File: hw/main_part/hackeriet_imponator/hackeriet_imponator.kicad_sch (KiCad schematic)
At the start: 9 parts, among them U1 ATmega328PB-A

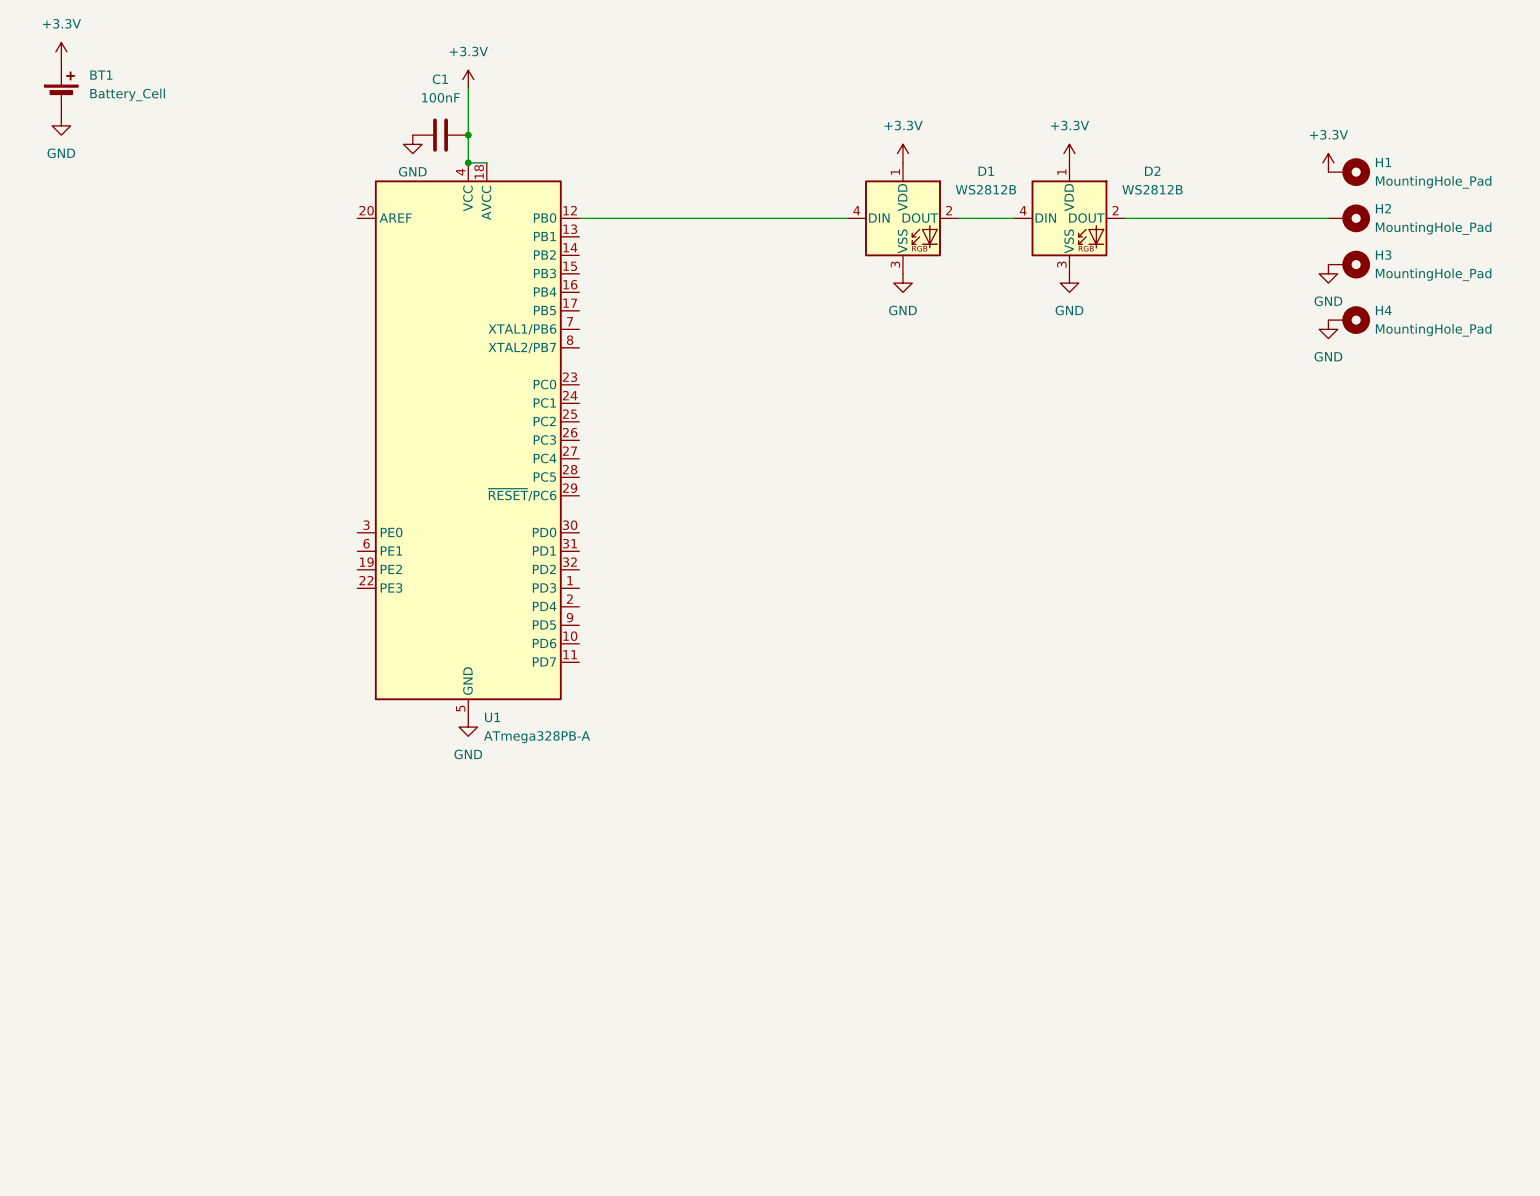
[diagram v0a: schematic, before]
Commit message: Added ring. Added programming header. Started with batt connector
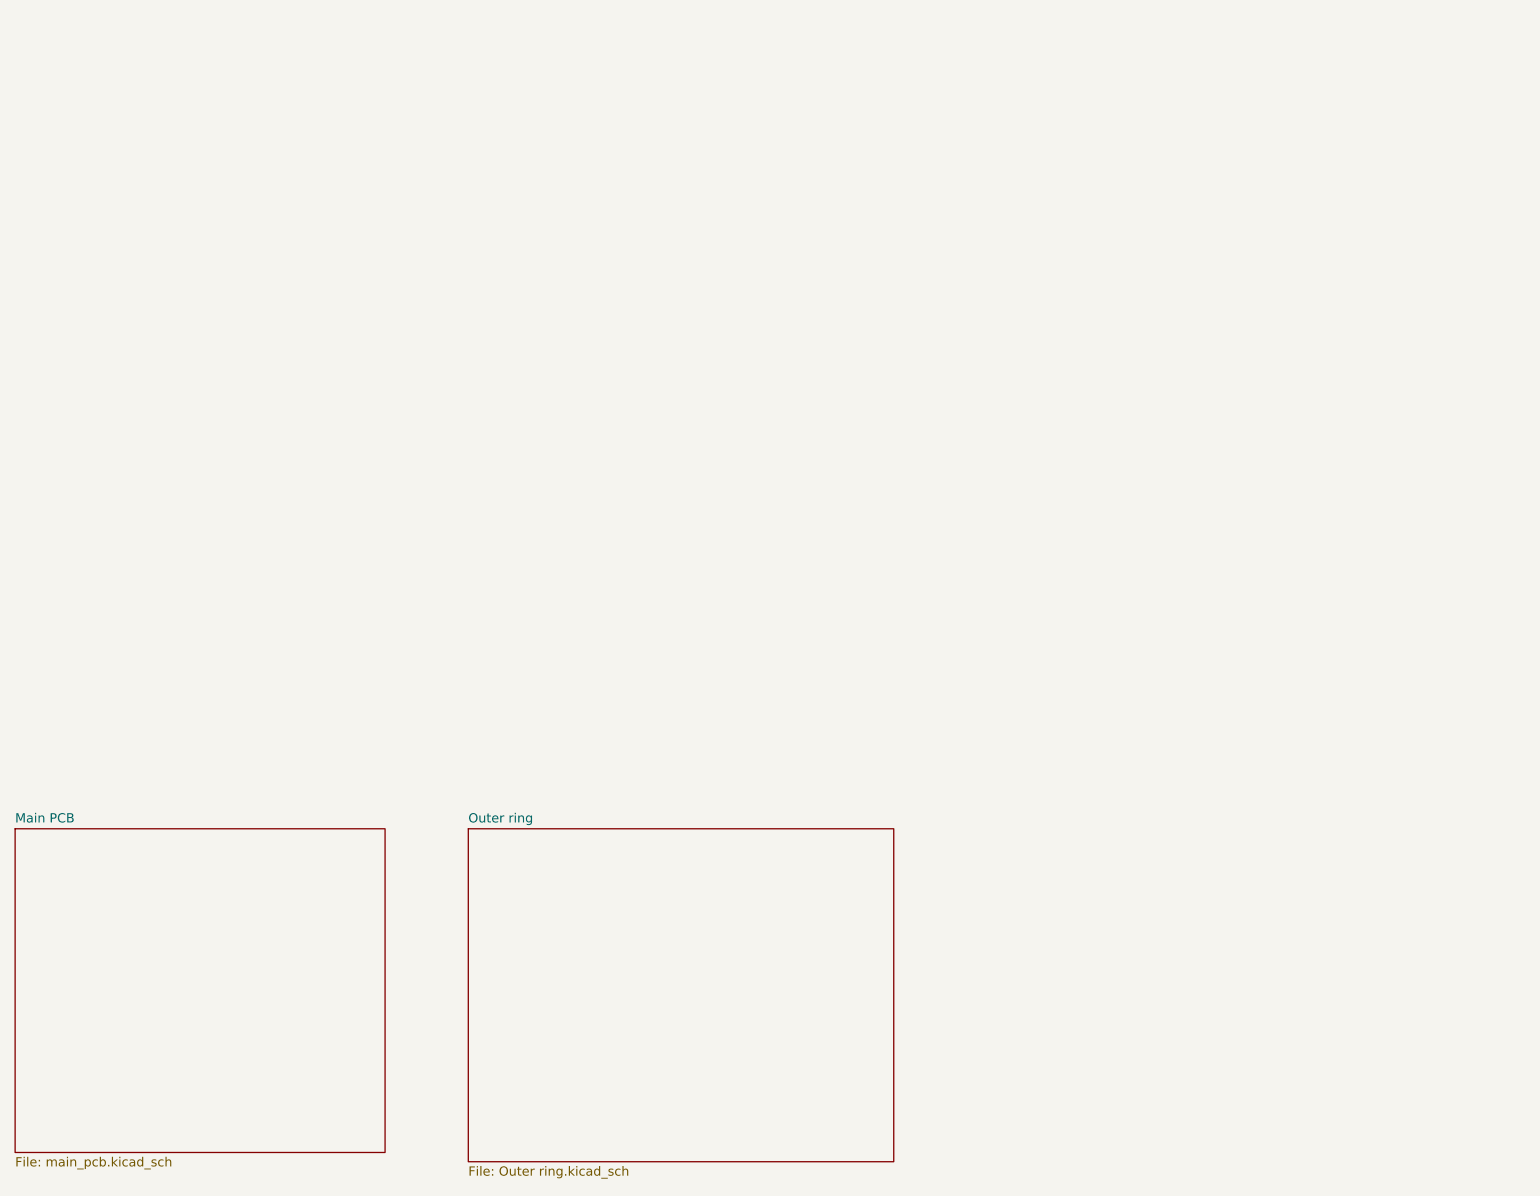
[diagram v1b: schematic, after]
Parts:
- removed BT1: Battery_Cell, symbol Device:Battery_Cell
- removed C1: 100nF, Capacitor_SMD:C_0603_1608Metric_Pad1.08x0.95mm_HandSolder, symbol Device:C
- removed D1, D2: WS2812B, LED_SMD:LED_WS2812B_PLCC4_5.0x5.0mm_P3.2mm, symbol LED:WS2812B
- removed H1, H2, H3, H4: MountingHole_Pad, MountingHole:MountingHole_3.2mm_M3_Pad_Via, symbol Mechanical:MountingHole_Pad
- removed U1: ATmega328PB-A, Package_QFP:TQFP-32_7x7mm_P0.8mm, symbol MCU_Microchip_ATmega:ATmega328PB-A
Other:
- added sheet Main PCB (main_pcb.kicad_sch)
- added sheet Outer ring (Outer ring.kicad_sch)
